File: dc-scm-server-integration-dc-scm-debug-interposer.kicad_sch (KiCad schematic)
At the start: 0 parts

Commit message: [#100720] Route DC-SCM connectors on schematic
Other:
- added sheet DC-SCI edge connector (edge-connector.kicad_sch)
- added sheet DC-SCI gold fingers connector (gold-fingers-connector.kicad_sch)
- added sheet Peripherals (peripherals.kicad_sch)
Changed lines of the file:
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@@
 		(comment 1 "www.antmicro.com")
+	)
+	(sheet
+		(at 193.04 99.06)
+		(size 45.72 161.29)
+		(exclude_from_sim no)
+		(in_bom yes)
+		(on_board yes)
+		(dnp no)
+		(fields_autoplaced yes)
+		(stroke
+			(width 0.1524)
+			(type solid)
+		)
+		(fill
+			(color 0 0 0 0)
+		)
+		(property "Sheetname" "DC-SCI gold fingers connector"
+			(at 193.04 98.3484 0)
+			(show_name no)
+			(do_not_autoplace no)
+			(effects
+				(font
+					(size 1.27 1.27)
+				)
+				(justify left bottom)
+			)
+		)
+		(property "Sheetfile" "gold-fingers-connector.kicad_sch"
+			(at 193.04 260.9346 0)
+			(show_name no)
+			(do_not_autoplace no)
+			(effects
+				(font
+					(size 1.27 1.27)
+				)
+				(justify left top)
+			)
+		)
+		(instances
+			(project "dc-scm-server-integration-dc-scm-debug-interposer"
+				(path "/4e753ac4-580e-447a-b828-7025703de482"
+					(page "2")
+				)
+			)
+		)
+	)
+	(sheet
+		(at 44.45 97.79)
+		(size 50.8 160.02)
+		(exclude_from_sim no)
+		(in_bom yes)
+		(on_board yes)
+		(dnp no)
+		(fields_autoplaced yes)
+		(stroke
+			(width 0.1524)
+			(type solid)
+		)
+		(fill
+			(color 0 0 0 0)
+		)
+		(property "Sheetname" "DC-SCI edge connector"
+			(at 44.45 97.0784 0)
+			(show_name no)
+			(do_not_autoplace no)
+			(effects
+				(font
+					(size 1.27 1.27)
+				)
+				(justify left bottom)
+			)
+		)
+		(property "Sheetfile" "edge-connector.kicad_sch"
+			(at 44.45 258.3946 0)
+			(show_name no)
+			(do_not_autoplace no)
+			(effects
+				(font
+					(size 1.27 1.27)
+				)
+				(justify left top)
+			)
+		)
+		(instances
+			(project "dc-scm-server-integration-dc-scm-debug-interposer"
+				(path "/4e753ac4-580e-447a-b828-7025703de482"
+					(page "3")
+				)
+			)
+		)
+	)
+	(sheet
+		(at 196.85 49.53)
+		(size 36.83 22.86)
+		(exclude_from_sim no)
+		(in_bom yes)
+		(on_board yes)
+		(dnp no)
+		(fields_autoplaced yes)
+		(stroke
+			(width 0.1524)
+			(type solid)
+		)
+		(fill
+			(color 0 0 0 0)
+		)
+		(property "Sheetname" "Peripherals"
+			(at 196.85 48.8184 0)
+			(show_name no)
+			(do_not_autoplace no)
+			(effects
+				(font
+					(size 1.27 1.27)
+				)
+				(justify left bottom)
+			)
+		)
+		(property "Sheetfile" "peripherals.kicad_sch"
+			(at 196.85 72.9746 0)
+			(show_name no)
+			(do_not_autoplace no)
+			(effects
+				(font
+					(size 1.27 1.27)
+				)
+				(justify left top)
+			)
+		)
+		(instances
+			(project "dc-scm-server-integration-dc-scm-debug-interposer"
+				(path "/4e753ac4-580e-447a-b828-7025703de482"
+					(page "4")
+				)
+			)
+		)
 	)
 	(sheet_instances

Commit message: [#100720] Add DCDC
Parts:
- added FD1, FD2, FD3, FD4, FD5, FD6, FD7, FD8: Fiducial_1mm_Mask2mm, antmicro-footprints:Fiducial_1mm_Mask2mm, symbol antmicroFiducialMarks:Fiducial_1mm_Mask2mm
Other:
- added sheet Flash (flash.kicad_sch)

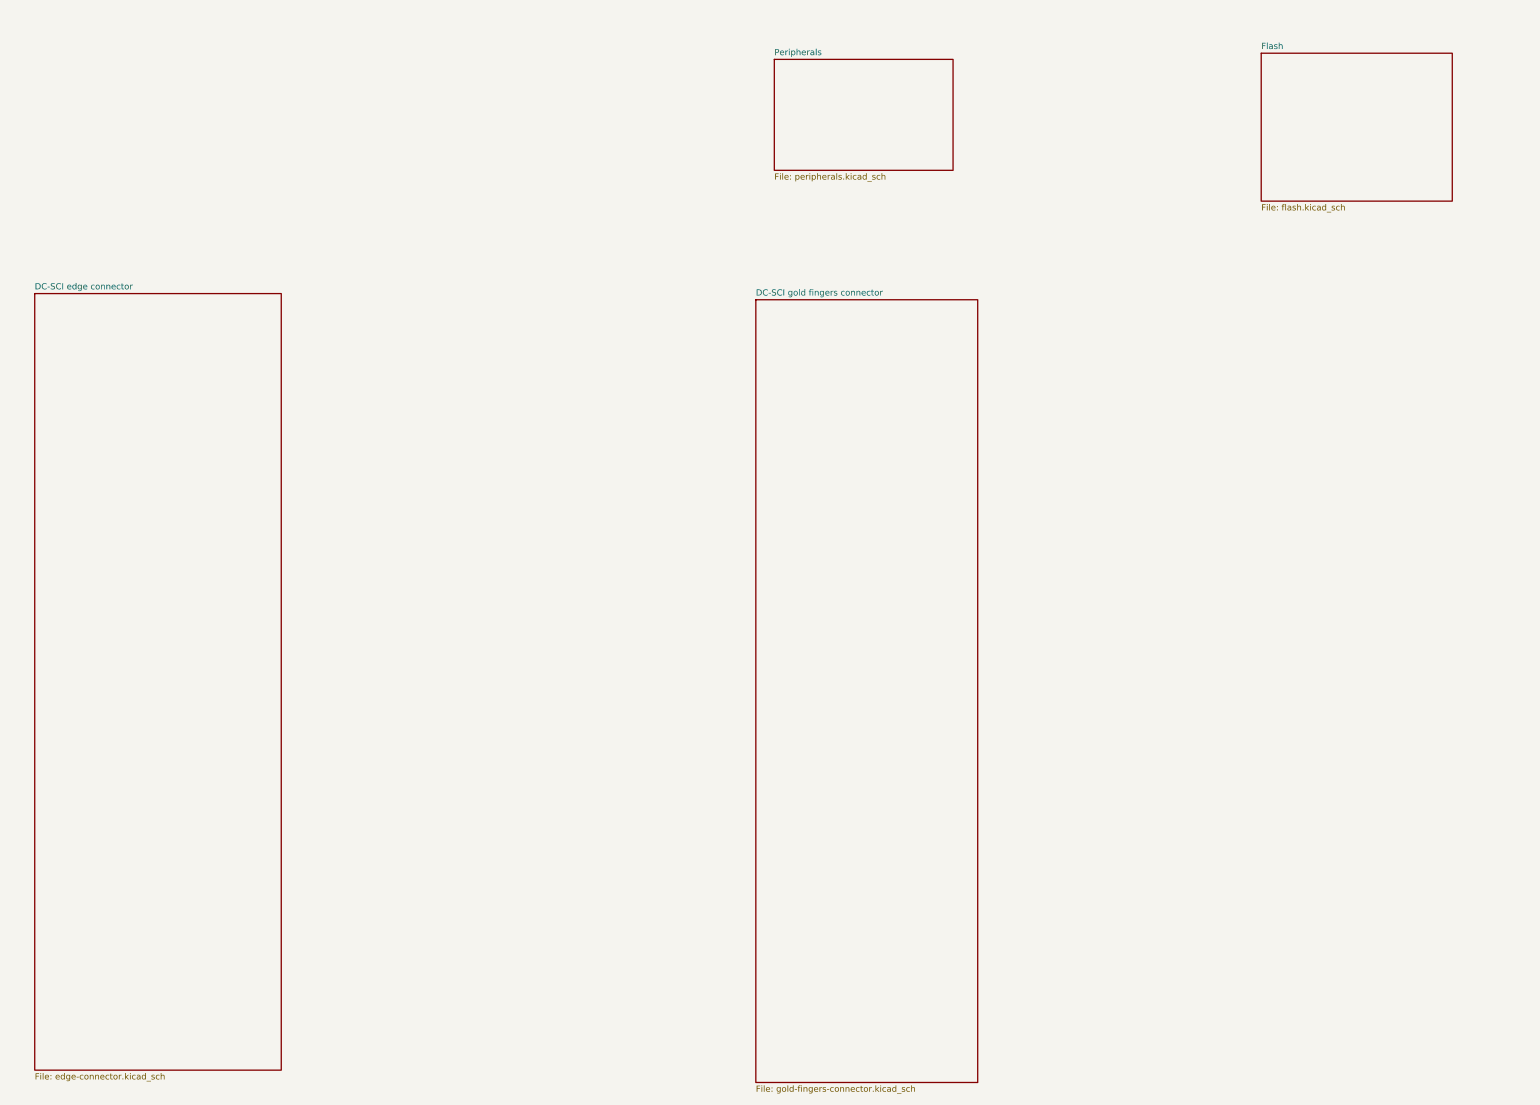
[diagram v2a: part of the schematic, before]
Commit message: [#100720] Finish schematic, clean ERC
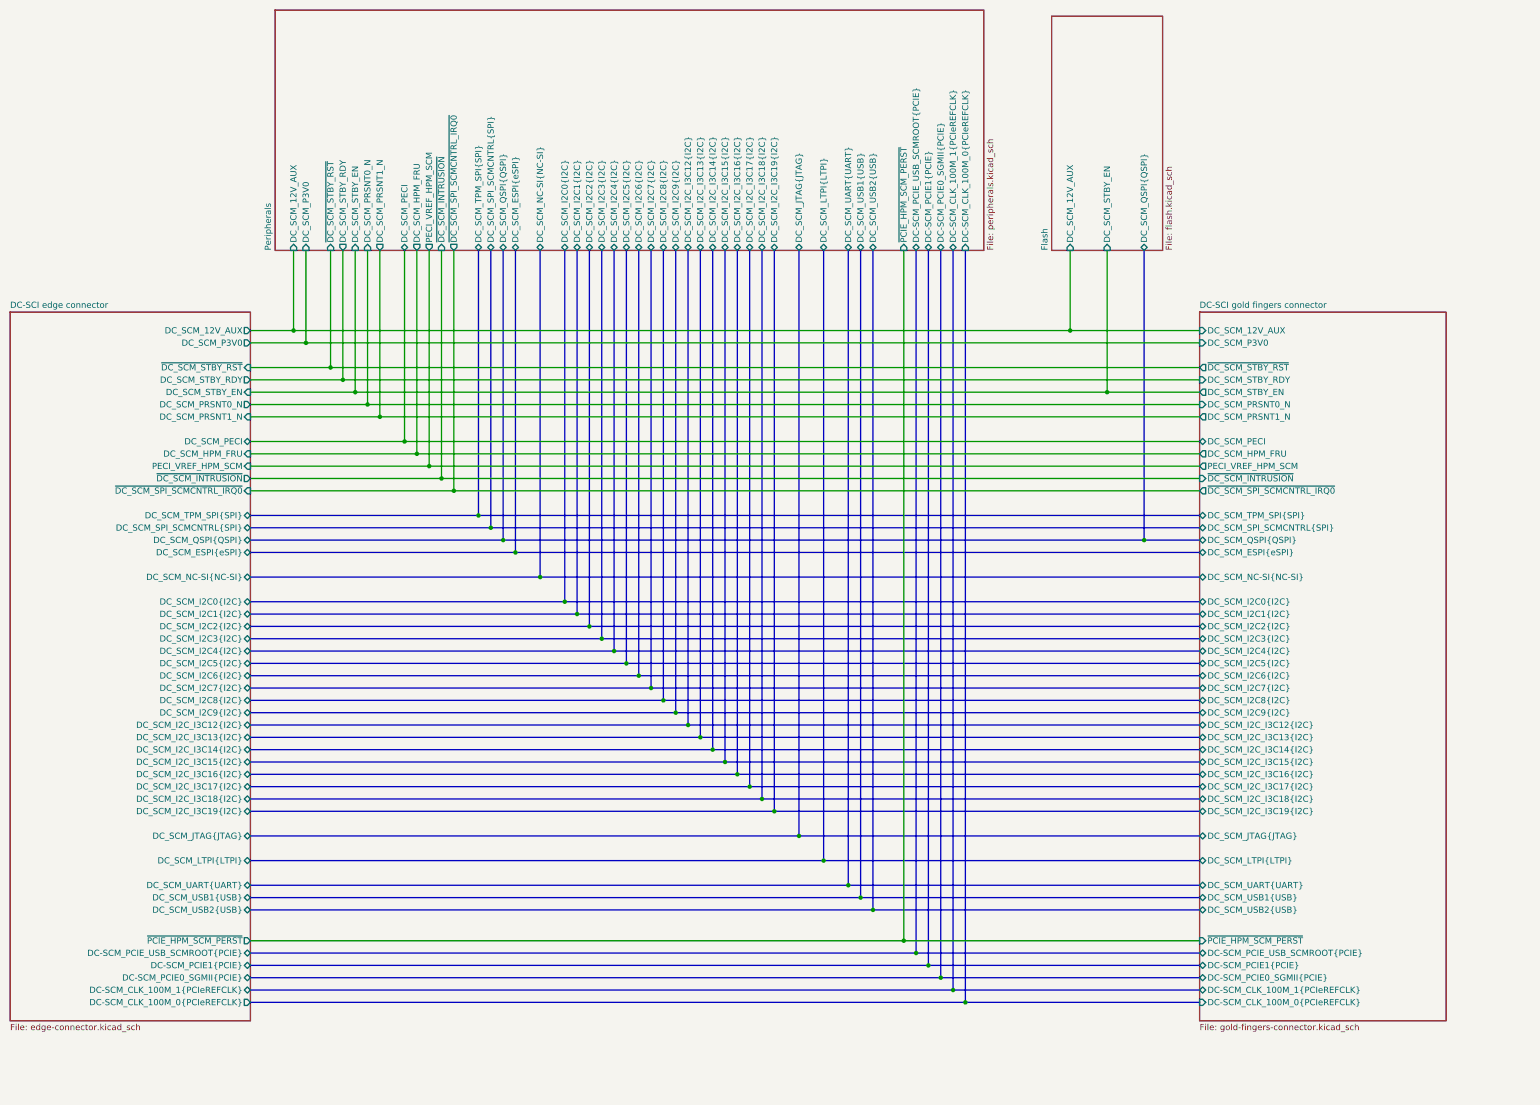
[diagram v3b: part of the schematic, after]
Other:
- sheet DC-SCI edge connector ports: added DC-SCM_CLK_100M_0{PCIeREFCLK}, DC-SCM_CLK_100M_1{PCIeREFCLK}, DC-SCM_PCIE0_SGMII{PCIE}, DC-SCM_PCIE1{PCIE}, DC-SCM_PCIE_USB_SCMROOT{PCIE}, DC_SCM_12V_AUX, DC_SCM_ESPI{eSPI}, DC_SCM_HPM_FRU, DC_SCM_I2C0{I2C}, DC_SCM_I2C1{I2C}, DC_SCM_I2C2{I2C}, DC_SCM_I2C3{I2C}, DC_SCM_I2C4{I2C}, DC_SCM_I2C5{I2C}, DC_SCM_I2C6{I2C}, DC_SCM_I2C7{I2C}, DC_SCM_I2C8{I2C}, DC_SCM_I2C9{I2C}, DC_SCM_I2C_I3C12{I2C}, DC_SCM_I2C_I3C13{I2C}, DC_SCM_I2C_I3C14{I2C}, DC_SCM_I2C_I3C15{I2C}, DC_SCM_I2C_I3C16{I2C}, DC_SCM_I2C_I3C17{I2C}, DC_SCM_I2C_I3C18{I2C}, DC_SCM_I2C_I3C19{I2C}, DC_SCM_JTAG{JTAG}, DC_SCM_LTPI{LTPI}, DC_SCM_NC-SI{NC-SI}, DC_SCM_P3V0, DC_SCM_PECI, DC_SCM_PRSNT0_N, DC_SCM_PRSNT1_N, DC_SCM_QSPI{QSPI}, DC_SCM_SPI_SCMCNTRL{SPI}, DC_SCM_STBY_EN, DC_SCM_STBY_RDY, DC_SCM_TPM_SPI{SPI}, DC_SCM_UART{UART}, DC_SCM_USB1{USB}, DC_SCM_USB2{USB}, PECI_VREF_HPM_SCM, ~{DC_SCM_INTRUSION}, ~{DC_SCM_SPI_SCMCNTRL_IRQ0}, ~{DC_SCM_STBY_RST}, ~{PCIE_HPM_SCM_PERST}; removed none
- sheet DC-SCI gold fingers connector ports: added DC-SCM_CLK_100M_0{PCIeREFCLK}, DC-SCM_CLK_100M_1{PCIeREFCLK}, DC-SCM_PCIE0_SGMII{PCIE}, DC-SCM_PCIE1{PCIE}, DC-SCM_PCIE_USB_SCMROOT{PCIE}, DC_SCM_12V_AUX, DC_SCM_ESPI{eSPI}, DC_SCM_HPM_FRU, DC_SCM_I2C0{I2C}, DC_SCM_I2C1{I2C}, DC_SCM_I2C2{I2C}, DC_SCM_I2C3{I2C}, DC_SCM_I2C4{I2C}, DC_SCM_I2C5{I2C}, DC_SCM_I2C6{I2C}, DC_SCM_I2C7{I2C}, DC_SCM_I2C8{I2C}, DC_SCM_I2C9{I2C}, DC_SCM_I2C_I3C12{I2C}, DC_SCM_I2C_I3C13{I2C}, DC_SCM_I2C_I3C14{I2C}, DC_SCM_I2C_I3C15{I2C}, DC_SCM_I2C_I3C16{I2C}, DC_SCM_I2C_I3C17{I2C}, DC_SCM_I2C_I3C18{I2C}, DC_SCM_I2C_I3C19{I2C}, DC_SCM_JTAG{JTAG}, DC_SCM_LTPI{LTPI}, DC_SCM_NC-SI{NC-SI}, DC_SCM_P3V0, DC_SCM_PECI, DC_SCM_PRSNT0_N, DC_SCM_PRSNT1_N, DC_SCM_QSPI{QSPI}, DC_SCM_SPI_SCMCNTRL{SPI}, DC_SCM_STBY_EN, DC_SCM_STBY_RDY, DC_SCM_TPM_SPI{SPI}, DC_SCM_UART{UART}, DC_SCM_USB1{USB}, DC_SCM_USB2{USB}, PECI_VREF_HPM_SCM, ~{DC_SCM_INTRUSION}, ~{DC_SCM_SPI_SCMCNTRL_IRQ0}, ~{DC_SCM_STBY_RST}, ~{PCIE_HPM_SCM_PERST}; removed none
- sheet Flash ports: added DC_SCM_12V_AUX, DC_SCM_QSPI{QSPI}, DC_SCM_STBY_EN; removed none
- sheet Peripherals ports: added DC-SCM_CLK_100M_0{PCIeREFCLK}, DC-SCM_CLK_100M_1{PCIeREFCLK}, DC-SCM_PCIE0_SGMII{PCIE}, DC-SCM_PCIE1{PCIE}, DC-SCM_PCIE_USB_SCMROOT{PCIE}, DC_SCM_12V_AUX, DC_SCM_ESPI{eSPI}, DC_SCM_HPM_FRU, DC_SCM_I2C0{I2C}, DC_SCM_I2C1{I2C}, DC_SCM_I2C2{I2C}, DC_SCM_I2C3{I2C}, DC_SCM_I2C4{I2C}, DC_SCM_I2C5{I2C}, DC_SCM_I2C6{I2C}, DC_SCM_I2C7{I2C}, DC_SCM_I2C8{I2C}, DC_SCM_I2C9{I2C}, DC_SCM_I2C_I3C12{I2C}, DC_SCM_I2C_I3C13{I2C}, DC_SCM_I2C_I3C14{I2C}, DC_SCM_I2C_I3C15{I2C}, DC_SCM_I2C_I3C16{I2C}, DC_SCM_I2C_I3C17{I2C}, DC_SCM_I2C_I3C18{I2C}, DC_SCM_I2C_I3C19{I2C}, DC_SCM_JTAG{JTAG}, DC_SCM_LTPI{LTPI}, DC_SCM_NC-SI{NC-SI}, DC_SCM_P3V0, DC_SCM_PECI, DC_SCM_PRSNT0_N, DC_SCM_PRSNT1_N, DC_SCM_QSPI{QSPI}, DC_SCM_SPI_SCMCNTRL{SPI}, DC_SCM_STBY_EN, DC_SCM_STBY_RDY, DC_SCM_TPM_SPI{SPI}, DC_SCM_UART{UART}, DC_SCM_USB1{USB}, DC_SCM_USB2{USB}, PECI_VREF_HPM_SCM, ~{DC_SCM_INTRUSION}, ~{DC_SCM_SPI_SCMCNTRL_IRQ0}, ~{DC_SCM_STBY_RST}, ~{PCIE_HPM_SCM_PERST}; removed none

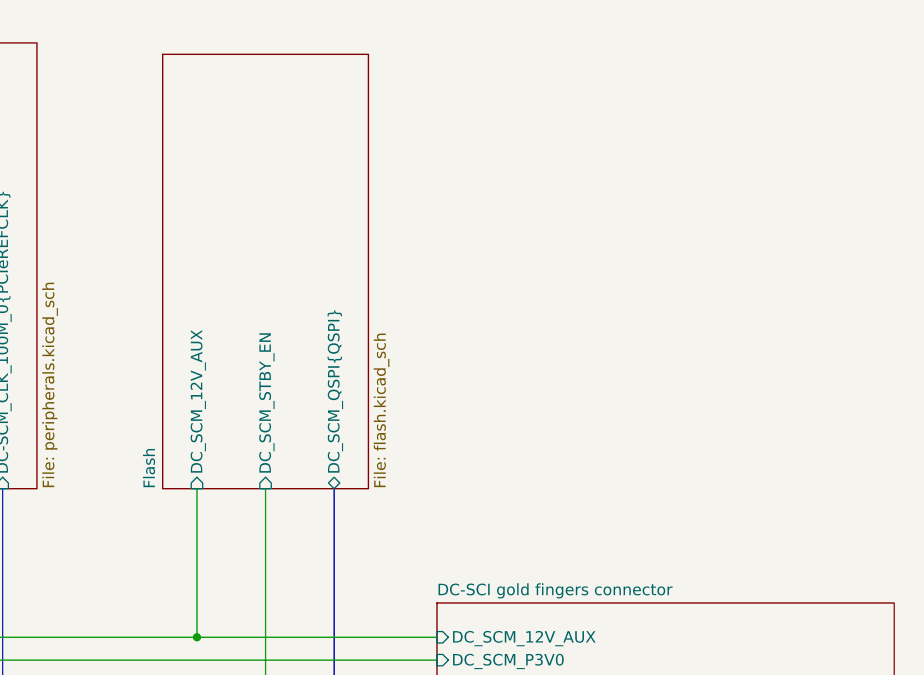
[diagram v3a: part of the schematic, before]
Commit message: [#100720] Start adding USB to schematic
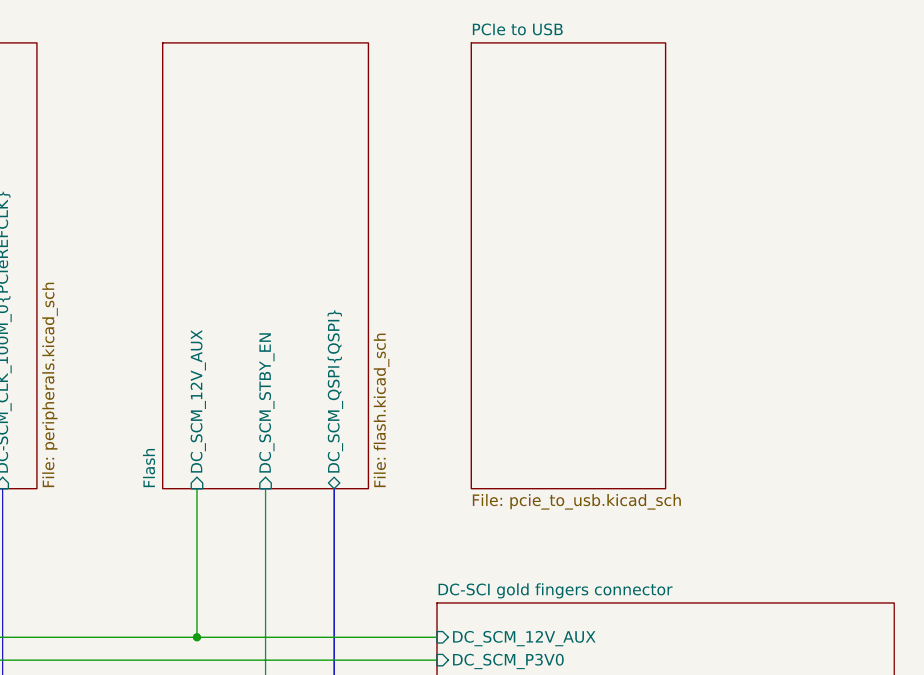
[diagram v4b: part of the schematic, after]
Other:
- added sheet PCIe to USB (pcie_to_usb.kicad_sch)
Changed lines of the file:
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@@
 	)
 	(sheet
-		(at 254 40.64)
-		(size 22.86 48.26)
+		(at 254 39.37)
+		(size 22.86 49.53)
 		(exclude_from_sim no)
 		(in_bom yes)
@@
 				)
 			)
+		)
+	)
+	(sheet
+		(at 288.29 39.37)
+		(size 21.59 49.53)
+		(exclude_from_sim no)
+		(in_bom yes)
+		(on_board yes)
+		(dnp no)
+		(fields_autoplaced yes)
+		(stroke
+			(width 0.1524)
+			(type solid)
+		)
+		(fill
+			(color 0 0 0 0)
+		)
+		(property "Sheetname" "PCIe to USB"
+			(at 288.29 38.6584 0)
+			(show_name no)
+			(do_not_autoplace no)
+			(effects
+				(font
+					(size 1.27 1.27)
+				)
+				(justify left bottom)
+			)
+		)
+		(property "Sheetfile" "pcie_to_usb.kicad_sch"
+			(at 288.29 89.4846 0)
+			(show_name no)
+			(do_not_autoplace no)
+			(effects
+				(font
+					(size 1.27 1.27)
+				)
+				(justify left top)
+			)
+		)
+		(instances
+			(project "dc-scm-server-integration-dc-scm-debug-interposer"
+				(path "/4e753ac4-580e-447a-b828-7025703de482"
+					(page "6")
+				)
+			)

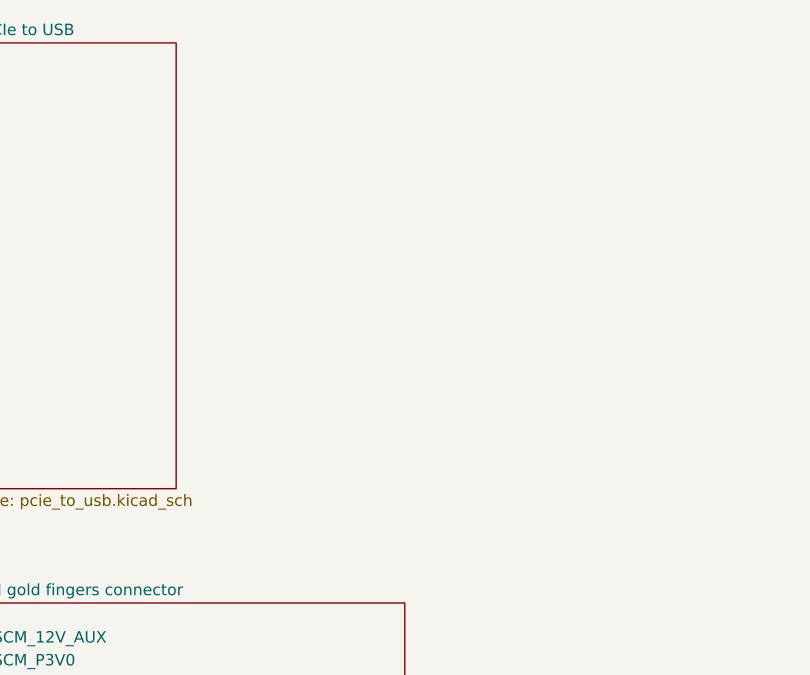
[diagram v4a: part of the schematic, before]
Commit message: [#100720] Add power section for PCIe to USB to schematic
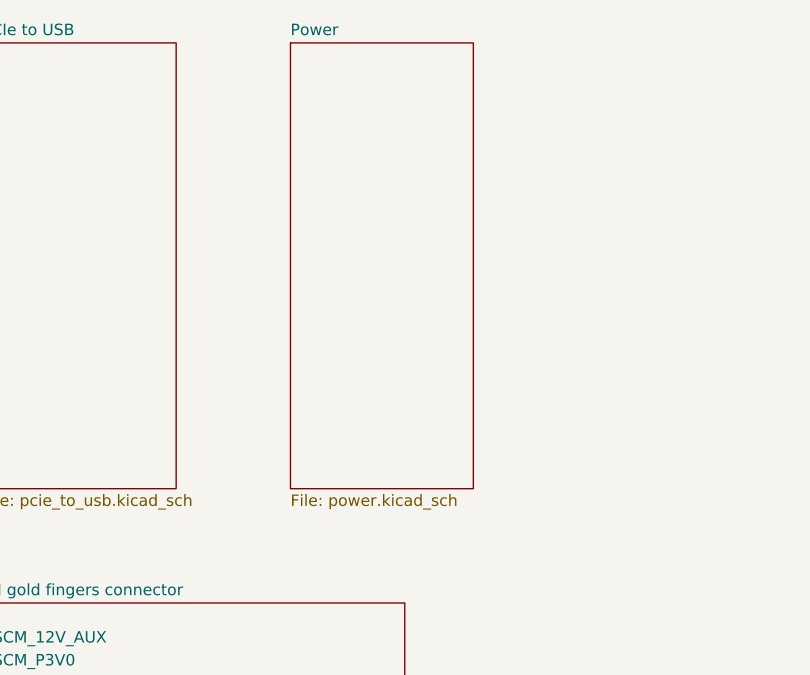
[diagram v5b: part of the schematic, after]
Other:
- added sheet Power (power.kicad_sch)
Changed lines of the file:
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@@
+		)
+	)
+	(sheet
+		(at 322.58 39.37)
+		(size 20.32 49.53)
+		(exclude_from_sim no)
+		(in_bom yes)
+		(on_board yes)
+		(dnp no)
+		(fields_autoplaced yes)
+		(stroke
+			(width 0.1524)
+			(type solid)
+		)
+		(fill
+			(color 0 0 0 0)
+		)
+		(property "Sheetname" "Power"
+			(at 322.58 38.6584 0)
+			(show_name no)
+			(do_not_autoplace no)
+			(effects
+				(font
+					(size 1.27 1.27)
+				)
+				(justify left bottom)
+			)
+		)
+		(property "Sheetfile" "power.kicad_sch"
+			(at 322.58 89.4846 0)
+			(show_name no)
+			(do_not_autoplace no)
+			(effects
+				(font
+					(size 1.27 1.27)
+				)
+				(justify left top)
+			)
+		)
+		(instances
+			(project "dc-scm-server-integration-dc-scm-debug-interposer"
+				(path "/4e753ac4-580e-447a-b828-7025703de482"
+					(page "7")
+				)
+			)
 		)
 	)
